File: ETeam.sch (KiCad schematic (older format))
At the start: 13 parts, among them J1 C1-, J2 C12+, J3 C24+, P1 BUS_OUT, P10 T29-32, P2 BUS_IN, P3 T1-4, P4 T5-8, P5 T9-12, P6 T13-16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

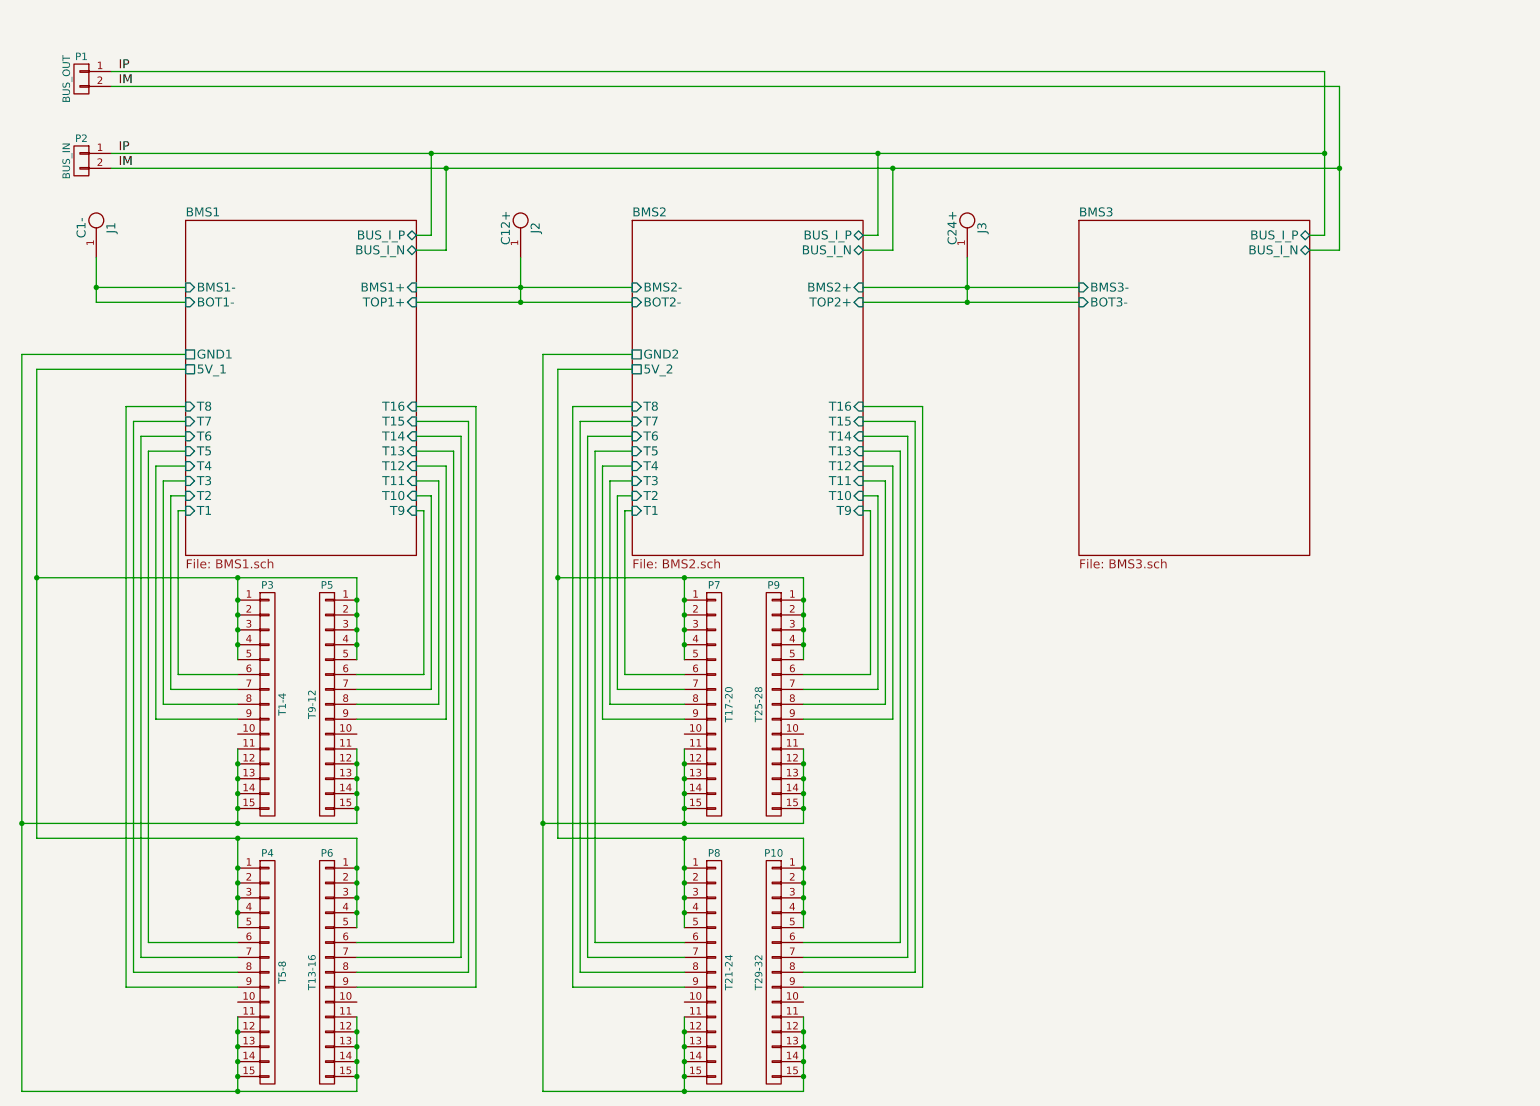
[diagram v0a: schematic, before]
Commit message: - changed the connectors for the temperature sensors
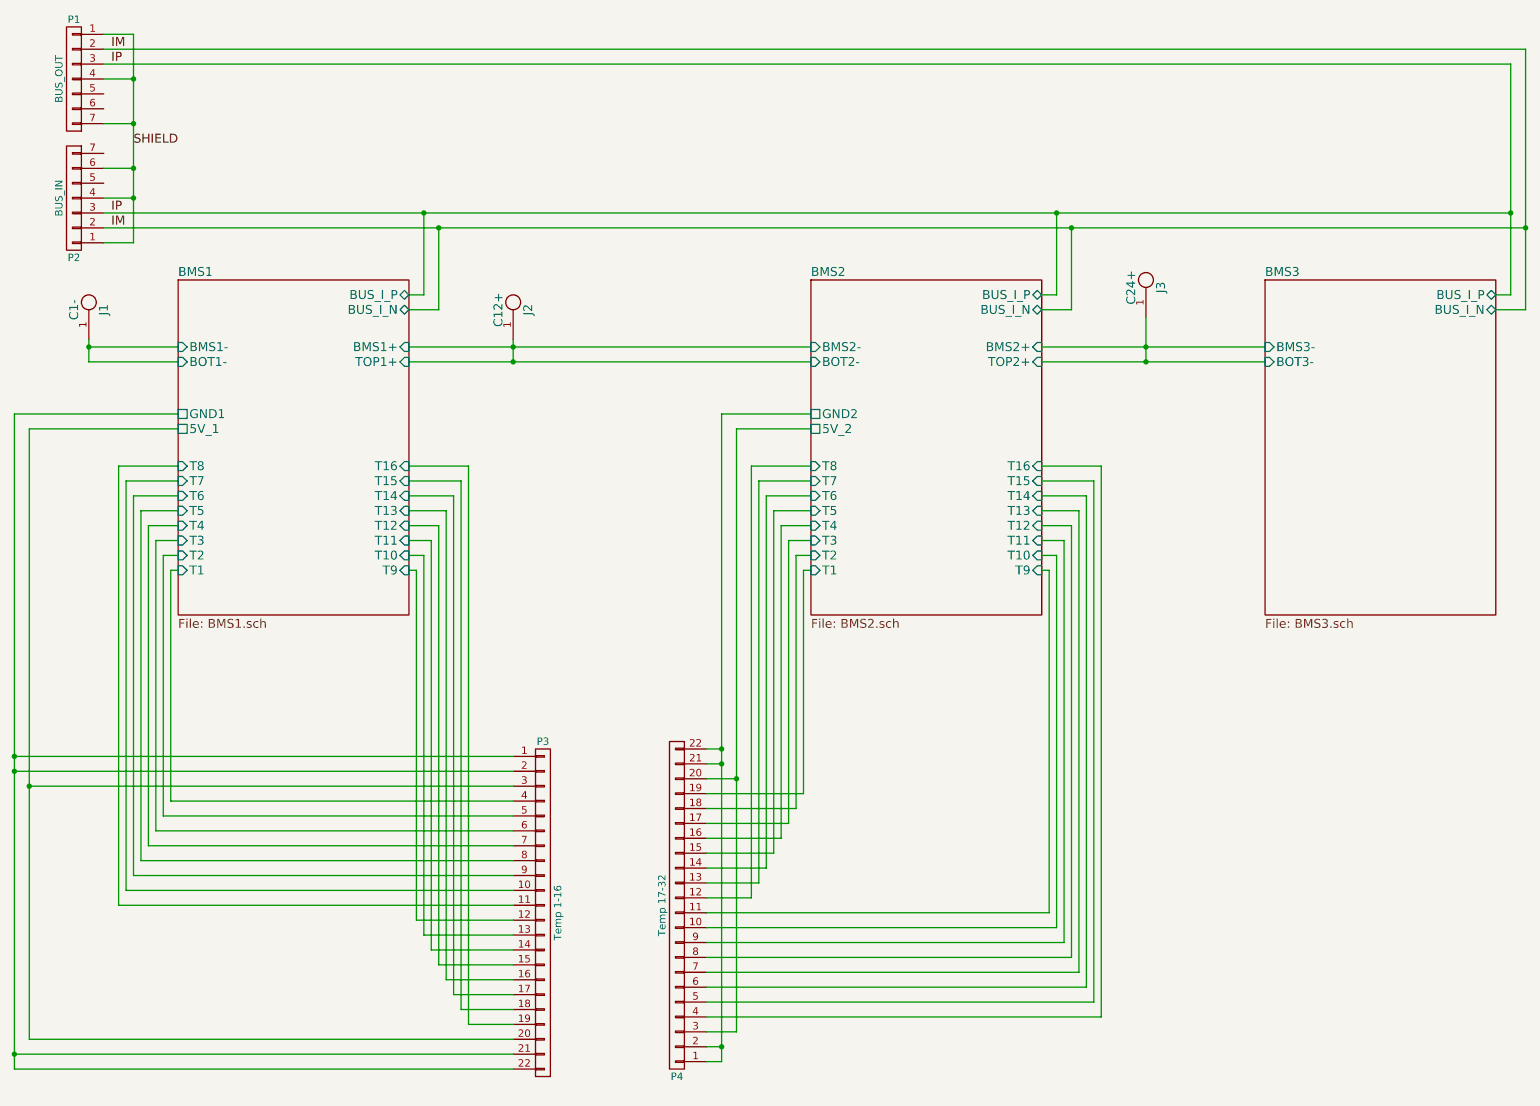
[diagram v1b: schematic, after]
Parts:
- removed P1: BUS_OUT, Connectors_Phoenix:PhoenixContact_MC-G_02x3.50mm_Angled, symbol CONN_01X02
- removed P10: T29-32, alexmod:DSUB15HD_90, symbol CONN_01X15
- removed P2: BUS_IN, Connectors_Phoenix:PhoenixContact_MC-G_02x3.50mm_Angled, symbol CONN_01X02
- removed P3: T1-4, alexmod:DSUB15HD_90, symbol CONN_01X15
- removed P4: T5-8, alexmod:DSUB15HD_90, symbol CONN_01X15
- removed P5: T9-12, alexmod:DSUB15HD_90, symbol CONN_01X15
- removed P6: T13-16, alexmod:DSUB15HD_90, symbol CONN_01X15
- removed P7: T17-20, alexmod:DSUB15HD_90, symbol CONN_01X15
- removed P8: T21-24, alexmod:DSUB15HD_90, symbol CONN_01X15
- removed P9: T25-28, alexmod:DSUB15HD_90, symbol CONN_01X15
- added P1: BUS_OUT, alexmod:Molex_0678007001, symbol CONN_01X07
- added P2: BUS_IN, alexmod:Molex_0678007001, symbol CONN_01X07
- added P3: Temp 1-16, alexmod:Ampenol_HFW22R, symbol CONN_01X22
- added P4: Temp 17-32, alexmod:Ampenol_HFW22R, symbol CONN_01X22
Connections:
- net BMS1/5V_1: now also P3.20 (P20), P3.3 (P3)
- net BMS1/GND1: now also P3.1 (P1), P3.2 (P2), P3.21 (P21), P3.22 (P22)
- net BMS1/T1: now also P3.4 (P4)
- net BMS1/T10: now also P3.13 (P13)
- net BMS1/T11: now also P3.14 (P14)
- net BMS1/T12: now also P3.15 (P15)
- net BMS1/T13: now also P3.16 (P16)
- net BMS1/T14: now also P3.17 (P17)
- net BMS1/T15: now also P3.18 (P18)
- net BMS1/T16: now also P3.19 (P19)
- net BMS1/T2: now also P3.5 (P5)
- net BMS1/T3: now also P3.6 (P6)
- net BMS1/T4: now also P3.7 (P7)
- net BMS1/T5: now also P3.8 (P8)
- net BMS1/T6: now also P3.9 (P9)
- net BMS1/T7: now also P3.10 (P10)
- net BMS1/T8: now also P3.11 (P11)
- net BMS1/T9: now also P3.12 (P12)
- net BMS2/5V_2: now also P4.20 (P20), P4.3 (P3)
- net BMS2/GND2: now also P4.1 (P1), P4.2 (P2), P4.21 (P21), P4.22 (P22)
- net BMS2/T1: now also P4.19 (P19)
- net BMS2/T10: now also P4.10 (P10)
- net BMS2/T11: now also P4.9 (P9)
- net BMS2/T12: now also P4.8 (P8)
- net BMS2/T13: now also P4.7 (P7)
- net BMS2/T14: now also P4.6 (P6)
- net BMS2/T15: now also P4.5 (P5)
- net BMS2/T16: now also P4.4 (P4)
- net BMS2/T2: now also P4.18 (P18)
- net BMS2/T3: now also P4.17 (P17)
- net BMS2/T4: now also P4.16 (P16)
- net BMS2/T5: now also P4.15 (P15)
- net BMS2/T6: now also P4.14 (P14)
- net BMS2/T7: now also P4.13 (P13)
- net BMS2/T8: now also P4.12 (P12)
- net BMS2/T9: now also P4.11 (P11)
- net IM: now also P1.2 (P2), P2.2 (P2)
- net IP: now also P1.3 (P3), P2.3 (P3)
- new net SHIELD: P1.1 (P1), P1.4 (P4), P1.7 (P7), P2.1 (P1), P2.4 (P4), P2.6 (P6)
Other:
- moved on the sheet: J1, J2, J3
